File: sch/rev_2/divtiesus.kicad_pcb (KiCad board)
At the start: 2 copper layers, 76.5 x 56.9 mm, 45 parts, among them J1 JTAG, J2 Joystick, J3 SD_Card, SW1 RESET, SW2 NMI, SW3 SW_DIP_x02, U1 EPM240T100, U2 628128, U3 28C64, U4 ESP-12E, U5 LM1117MP-3.3, U6 74HCT165D, X1 24MHz

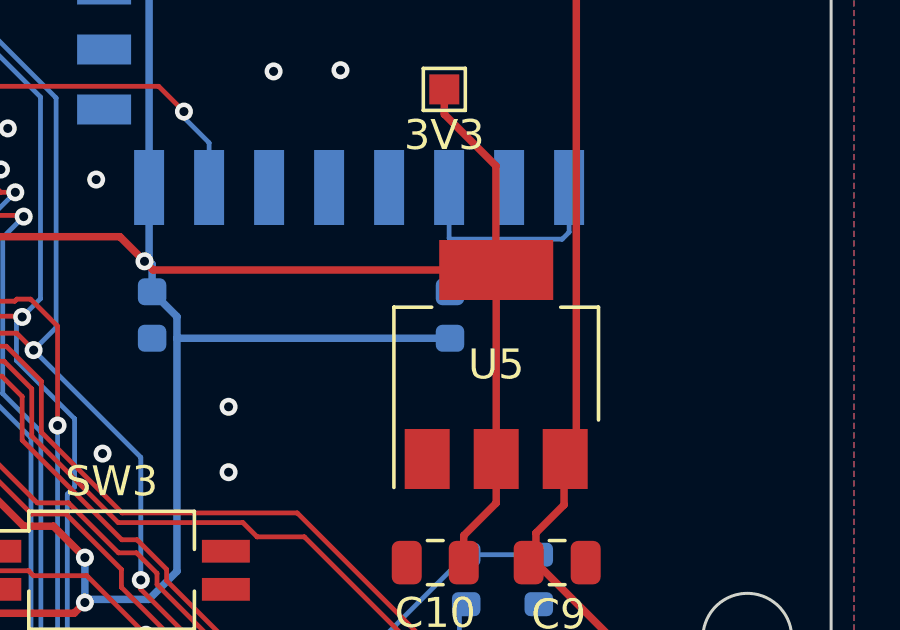
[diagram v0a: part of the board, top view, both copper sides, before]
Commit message: Cosmetic fix: change R1 footprint from C_0603 to R_0603 and update IBOM
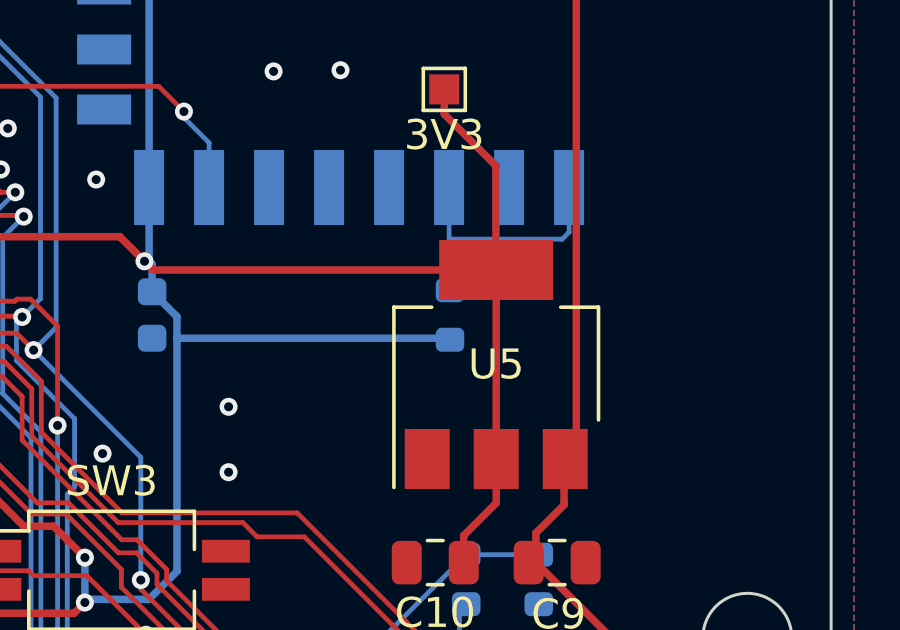
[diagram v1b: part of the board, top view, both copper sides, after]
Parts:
- R1: footprint Capacitor_SMD:C_0603_1608Metric -> Resistor_SMD:R_0603_1608Metric
- U2: value 628128 -> 628128
